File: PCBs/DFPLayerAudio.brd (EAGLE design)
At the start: 45.4 x 33 mm, 14 parts

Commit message: updated something
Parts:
- removed RXTXGND: JST-XH-03-PIN-LONG-PAD, Rembrandt Electronics - JST XH Connectors v1-0:JST-XH-03-PACKAGE-LONG-PAD
- added J2: JST-XH-04-PIN-LONG-PAD, Rembrandt Electronics - JST XH Connectors v1-0:JST-XH-04-PACKAGE-LONG-PAD
- J4: value 6V-12V -> Power
- renumbered 5V to J3, 6V-12V to J4, AMPLIFIER to J1, SPKR1 to LEFTSPKR, SPKR2 to RIGHTSPKR
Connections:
- new net N$6: DFPLAYER.16, J2.2
- new net N$7: J2.3
- net GND: now also J2.1; no longer RXTXGND.1
- net N$2: no longer RXTXGND.2
- net N$8: now also J2.4; no longer RXTXGND.3
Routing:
- net N$8: track 17.7 -> 15.2 mm
- net N$2: track 9.33 -> 8.06 mm
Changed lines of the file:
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@@
 </autorouter>
 <elements>
-<element name="6V-12V" library="SparkFun-Connectors" package="SCREWTERMINAL-5MM-2" value="6V-12V" x="76.2" y="2.54" smashed="yes" rot="R90">
+<element name="J4" library="SparkFun-Connectors" package="SCREWTERMINAL-5MM-2" value="Power" x="76.2" y="2.54" smashed="yes" rot="R90">
 <attribute name="NAME" x="81.28" y="3.81" size="1.27" layer="25" font="vector" ratio="10" rot="R90"/>
 <attribute name="SF_SKU" value="PRT-08432" x="130.81" y="24.13" size="1.778" layer="27" rot="R90" display="off"/>
@@
 <attribute name="VALUE" x="48.26" y="17.78" size="1.27" layer="27" rot="R270" align="top-center"/>
 </element>
-<element name="AMPLIFIER" library="Rembrandt Electronics - JST XH Connectors v1-0" package="JST-XH-03-PACKAGE-LONG-PAD" value="JST-XH-03-PIN-LONG-PAD" x="43.18" y="8.89" smashed="yes" rot="R270">
+<element name="J1" library="Rembrandt Electronics - JST XH Connectors v1-0" package="JST-XH-03-PACKAGE-LONG-PAD" value="JST-XH-03-PIN-LONG-PAD" x="43.18" y="8.89" smashed="yes" rot="R270">
 <attribute name="NAME" x="47.785" y="5.58" size="1.016" layer="25" ratio="10" rot="R90"/>
 <attribute name="VALUE" x="44.5325" y="21.1125" size="1.016" layer="27" ratio="10" rot="R270"/>
 </element>
-<element name="RXTXGND" library="Rembrandt Electronics - JST XH Connectors v1-0" package="JST-XH-03-PACKAGE-LONG-PAD" value="JST-XH-03-PIN-LONG-PAD" x="43.18" y="20.32" smashed="yes" rot="R270">
-<attribute name="NAME" x="47.785" y="17.01" size="1.016" layer="25" ratio="10" rot="R90"/>
-<attribute name="VALUE" x="44.5325" y="22.3825" size="1.016" layer="27" ratio="10" rot="R270"/>
-</element>
-<element name="SPKR1" library="Rembrandt Electronics - JST XH Connectors v1-0" package="JST-XH-02-PACKAGE-LONG-PAD" value="JST-XH-02-PIN-LONG-PAD" x="53.34" y="1.27" smashed="yes">
+<element name="LEFTSPKR" library="Rembrandt Electronics - JST XH Connectors v1-0" package="JST-XH-02-PACKAGE-LONG-PAD" value="JST-XH-02-PIN-LONG-PAD" x="53.34" y="1.27" smashed="yes">
 <attribute name="NAME" x="49.085" y="0.5" size="1.016" layer="25" ratio="10" rot="R90"/>
 <attribute name="VALUE" x="48.7675" y="5.1625" size="1.016" layer="27" ratio="10"/>
 </element>
-<element name="SPKR2" library="Rembrandt Electronics - JST XH Connectors v1-0" package="JST-XH-02-PACKAGE-LONG-PAD" value="JST-XH-02-PIN-LONG-PAD" x="62.23" y="1.27" smashed="yes">
+<element name="RIGHTSPKR" library="Rembrandt Electronics - JST XH Connectors v1-0" package="JST-XH-02-PACKAGE-LONG-PAD" value="JST-XH-02-PIN-LONG-PAD" x="62.23" y="1.27" smashed="yes">
 <attribute name="NAME" x="57.975" y="0.5" size="1.016" layer="25" ratio="10" rot="R90"/>
 <attribute name="VALUE" x="58.9275" y="5.1625" size="1.016" layer="27" ratio="10"/>
@@
 <attribute name="VALUE" x="49.276" y="31.496" size="1.27" layer="27" rot="R180"/>
 </element>
-<element name="5V" library="Rembrandt Electronics - JST XH Connectors v1-0" package="JST-XH-02-PACKAGE-LONG-PAD" value="JST-XH-02-PIN-LONG-PAD" x="81.28" y="12.7" smashed="yes" rot="R90">
+<element name="J3" library="Rembrandt Electronics - JST XH Connectors v1-0" package="JST-XH-02-PACKAGE-LONG-PAD" value="JST-XH-02-PIN-LONG-PAD" x="81.28" y="12.7" smashed="yes" rot="R90">
 <attribute name="NAME" x="83.32" y="8.445" size="1.016" layer="25" ratio="10" rot="R180"/>
 <attribute name="VALUE" x="77.3875" y="9.3975" size="1.016" layer="27" ratio="10" rot="R90"/>
@@
 <attribute name="NAME" x="48.006" y="25.654" size="1.27" layer="25" rot="R180"/>
 <attribute name="VALUE" x="48.006" y="28.956" size="1.27" layer="27" rot="R180"/>
+</element>
+<element name="J2" library="Rembrandt Electronics - JST XH Connectors v1-0" package="JST-XH-04-PACKAGE-LONG-PAD" value="JST-XH-04-PIN-LONG-PAD" x="48.26" y="-7.62" smashed="yes">
+<attribute name="NAME" x="41.605" y="-9.66" size="1.016" layer="25" ratio="10" rot="R90"/>
+<attribute name="VALUE" x="42.2575" y="-3.7275" size="1.016" layer="27" ratio="10"/>
 </element>
 </elements>
@@
 <signal name="GND">
 <contactref element="DFPLAYER" pad="10"/>
-<contactref element="SPKR1" pad="1"/>
-<contactref element="SPKR2" pad="1"/>
+<contactref element="LEFTSPKR" pad="1"/>
+<contactref element="RIGHTSPKR" pad="1"/>
 <contactref element="LED2" pad="C"/>
-<contactref element="6V-12V" pad="2"/>
+<contactref element="J4" pad="2"/>
 <contactref element="7805" pad="3"/>
 <contactref element="C4" pad="2"/>
 <contactref element="C3" pad="2"/>
-<contactref element="AMPLIFIER" pad="2"/>
+<contactref element="J1" pad="2"/>
 <contactref element="DFPLAYER" pad="7"/>
-<contactref element="RXTXGND" pad="1"/>
 <wire x1="73.0758" y1="27.7368" x2="73.0758" y2="26.67" width="0.6096" layer="1"/>
 <wire x1="73.6092" y1="28.2702" x2="73.0758" y2="27.7368" width="0.6096" layer="1"/>
@@
 <wire x1="45.8724" y1="11.2014" x2="45.8724" y2="20.8026" width="0.6096" layer="16"/>
 <wire x1="43.2054" y1="8.5344" x2="45.8724" y2="11.2014" width="0.6096" layer="16"/>
-<wire x1="43.2054" y1="22.4028" x2="43.18" y2="22.86" width="0.6096" layer="16"/>
 <wire x1="43.2054" y1="8.5344" x2="43.18" y2="8.89" width="0.6096" layer="16"/>
 <wire x1="61.341" y1="4.2672" x2="68.2752" y2="11.2014" width="0.6096" layer="16"/>
@@
 <wire x1="61.341" y1="1.6002" x2="60.96" y2="1.27" width="0.6096" layer="16"/>
 <via x="71.4756" y="1.6002" extent="1-16" drill="0.35"/>
-<contactref element="5V" pad="2"/>
+<contactref element="J3" pad="2"/>
 <wire x1="81.0768" y1="19.2024" x2="81.0768" y2="14.4018" width="0.6096" layer="1"/>
 <wire x1="80.01" y1="20.2692" x2="81.0768" y2="19.2024" width="0.6096" layer="1"/>
 <wire x1="81.0768" y1="14.4018" x2="81.28" y2="13.97" width="0.6096" layer="1"/>
 <wire x1="80.01" y1="20.2692" x2="79.97" y2="20.32" width="0.6096" layer="1"/>
+<contactref element="J2" pad="1"/>
+<wire x1="44.45" y1="-7.62" x2="52.07" y2="1.27" width="0" layer="19" extent="1-1"/>
 </signal>
 <signal name="VCC">
@@
 <wire x1="50.8" y1="26.67" x2="51.2064" y2="26.67" width="0.6096" layer="1"/>
 <wire x1="69.8754" y1="4.2672" x2="69.53" y2="3.81" width="0.6096" layer="1"/>
-<contactref element="5V" pad="1"/>
+<contactref element="J3" pad="1"/>
 <wire x1="79.4766" y1="11.2014" x2="81.0768" y2="11.2014" width="0.6096" layer="1"/>
 <wire x1="78.4098" y1="10.1346" x2="79.4766" y2="11.2014" width="0.6096" layer="1"/>
@@
 <signal name="N$14">
 <contactref element="DFPLAYER" pad="5"/>
-<contactref element="AMPLIFIER" pad="1"/>
+<contactref element="J1" pad="1"/>
 <wire x1="47.4726" y1="16.002" x2="50.673" y2="16.002" width="0.6096" layer="1"/>
 <wire x1="43.2054" y1="11.7348" x2="47.4726" y2="16.002" width="0.6096" layer="1"/>
@@
 <signal name="N$12">
 <contactref element="DFPLAYER" pad="8"/>
-<contactref element="SPKR1" pad="2"/>
+<contactref element="LEFTSPKR" pad="2"/>
 <wire x1="51.2064" y1="5.334" x2="51.2064" y2="8.5344" width="0.6096" layer="16"/>
 <wire x1="54.9402" y1="1.6002" x2="51.2064" y2="5.334" width="0.6096" layer="16"/>
@@
 <signal name="N$19">
 <contactref element="DFPLAYER" pad="6"/>
-<contactref element="SPKR2" pad="2"/>
+<contactref element="RIGHTSPKR" pad="2"/>
 <wire x1="61.341" y1="3.7338" x2="51.2064" y2="13.8684" width="0.6096" layer="1"/>
 <wire x1="61.8744" y1="3.7338" x2="61.341" y2="3.7338" width="0.6096" layer="1"/>
@@
 <signal name="N$3">
 <contactref element="7805" pad="1"/>
-<contactref element="6V-12V" pad="1"/>
+<contactref element="J4" pad="1"/>
 <contactref element="C3" pad="1"/>
 <wire x1="74.1426" y1="24.003" x2="74.1426" y2="26.67" width="0.6096" layer="1"/>
@@
 <signal name="N$8">
 <contactref element="R2" pad="2"/>
-<contactref element="RXTXGND" pad="3"/>
 <wire x1="44.196" y1="25.146" x2="44.8056" y2="24.5364" width="0.6096" layer="1"/>
 <wire x1="46.9392" y1="22.4028" x2="44.8056" y2="24.5364" width="0.6096" layer="16"/>
@@
 <wire x1="46.99" y1="21.2852" x2="46.99" y2="19.05" width="0.6096" layer="1"/>
 <wire x1="46.99" y1="19.05" x2="45.72" y2="17.78" width="0.6096" layer="1"/>
-<wire x1="45.72" y1="17.78" x2="43.18" y2="17.78" width="0.6096" layer="1"/>
+<contactref element="J2" pad="4"/>
+<wire x1="52.07" y1="-7.62" x2="45.72" y2="17.78" width="0" layer="19" extent="1-1"/>
 </signal>
 <signal name="N$1">
-<contactref element="AMPLIFIER" pad="3"/>
+<contactref element="J1" pad="3"/>
 <contactref element="DFPLAYER" pad="4"/>
 <wire x1="46.9392" y1="14.9352" x2="50.673" y2="18.669" width="0.6096" layer="16"/>
@@
 </signal>
 <signal name="N$2">
-<contactref element="RXTXGND" pad="2"/>
 <contactref element="R3" pad="2"/>
-<wire x1="43.18" y1="20.32" x2="44.45" y2="20.32" width="0.6096" layer="1"/>
 <wire x1="45.799" y1="21.669" x2="45.799" y2="21.8082875" width="0.6096" layer="1"/>
 <wire x1="46.99" y1="22.9992875" x2="46.99" y2="24.13" width="0.6096" layer="1"/>
@@
 <wire x1="49.53" y1="21.59" x2="50.8" y2="21.59" width="0.6096" layer="1"/>
 </signal>
+<signal name="N$7">
+<contactref element="J2" pad="3"/>
+</signal>
+<signal name="N$6">
+<contactref element="J2" pad="2"/>
+<contactref element="DFPLAYER" pad="16"/>
+<wire x1="46.99" y1="-7.62" x2="68.58" y2="26.67" width="0" layer="19" extent="1-1"/>
+</signal>
 </signals>

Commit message: audio board updated
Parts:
- moved J2 29.2 mm to (44.5, 21.3), turned to 90 degrees
- moved J3 4.31 mm to (78.2, 15.7)
- moved R2 4.19 mm to (52.3, 30.2)
- moved 7805 3.59 mm to (77.0, 23.9)
- moved C3 2.96 mm to (72.1, 29.2)
- moved R3 2.59 mm to (47.5, 29.2)
- moved C4 1.30 mm to (72.4, 14.2), turned to 270 degrees
- moved J4 1.02 mm to (77.2, 2.54)
- moved DFPLAYER 0.51 mm to (59.7, 18.3)
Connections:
- removed net N$2: R3.2
- net N$7: now also R3.2
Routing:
- net N$6: track 0.00 -> 32.4 mm
- net N$7: track 0.00 -> 8.52 mm
- net N$2: track 8.06 -> 0.00 mm
- net GND: track 137.8 -> 132.0 mm
- net VCC: track 66.5 -> 71.9 mm, vias 0 -> 1
- net N$5: track 12.8 -> 9.51 mm
- net N$3: track 28.3 -> 31.5 mm
- net N$4: track 7.01 -> 9.46 mm
- net N$8: track 15.2 -> 12.9 mm, vias 2 -> 0
- net N$1: track 16.8 -> 19.0 mm
- net N$12: track 9.49 -> 10.00 mm
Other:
- board size 45.4 x 33 mm -> 45.4 x 34 mm
- board text added: "Audio Shield V1.0"
- board text added: "Designed & Manufacturd by"
- board text added: "FutureBot"
- board text added: "PINWHEEL ROBOTICS"
- board text added: "Pinwheel Robotics"

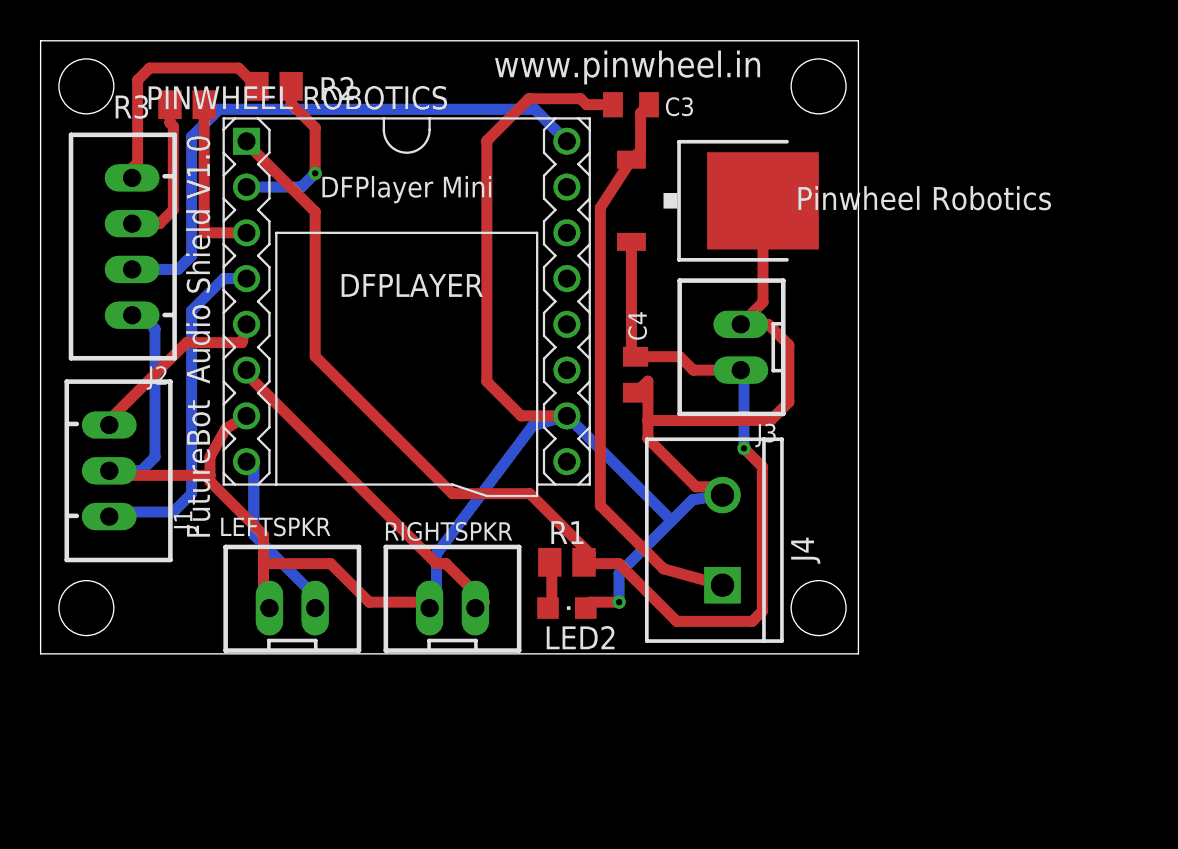
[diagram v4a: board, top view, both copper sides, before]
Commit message: naming part of audio board updated
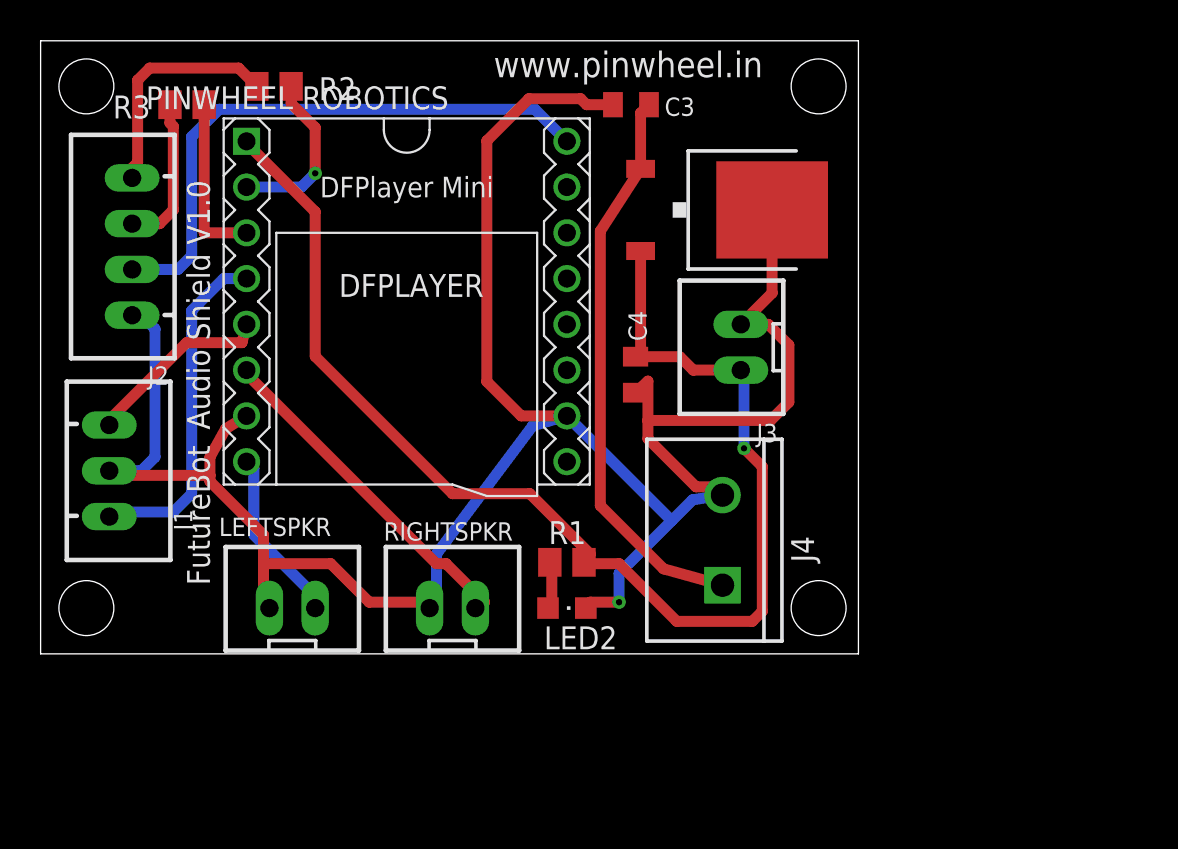
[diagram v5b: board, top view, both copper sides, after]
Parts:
- moved 7805 0.72 mm to (77.5, 23.4)
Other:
- board text added: "17/11/2021"
- board text added: "Documentation at"
- board text added: "FutureBot Audio Shield V1.0"
- board text added: "care@pinwheel.in"

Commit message: updated gerber and corrected few things
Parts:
- renumbered J1 to AMPLIFIER, J2 to UART, J3 to 5V, J4 to 7V-9V
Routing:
- added copper zone on layer 1, net GND
- added copper zone on layer 16, net GND
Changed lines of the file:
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@@
 </autorouter>
 <elements>
-<element name="J4" library="SparkFun-Connectors" package="SCREWTERMINAL-5MM-2" value="Power" x="77.216" y="2.54" smashed="yes" rot="R90">
+<element name="7V-9V" library="SparkFun-Connectors" package="SCREWTERMINAL-5MM-2" value="Power" x="77.216" y="2.54" smashed="yes" rot="R90">
 <attribute name="NAME" x="82.296" y="3.81" size="1.27" layer="25" font="vector" ratio="10" rot="R90"/>
 <attribute name="SF_SKU" value="PRT-08432" x="131.826" y="24.13" size="1.778" layer="27" rot="R90" display="off"/>
@@
 <attribute name="VALUE" x="48.26" y="18.288" size="1.27" layer="27" rot="R270" align="top-center"/>
 </element>
-<element name="J1" library="Rembrandt Electronics - JST XH Connectors v1-0" package="JST-XH-03-PACKAGE-LONG-PAD" value="JST-XH-03-PIN-LONG-PAD" x="43.18" y="8.89" smashed="yes" rot="R270">
-<attribute name="NAME" x="47.785" y="5.58" size="1.016" layer="25" ratio="10" rot="R90"/>
+<element name="AMPLIFIER" library="Rembrandt Electronics - JST XH Connectors v1-0" package="JST-XH-03-PACKAGE-LONG-PAD" value="JST-XH-03-PIN-LONG-PAD" x="43.18" y="8.89" smashed="yes" rot="R270">
+<attribute name="NAME" x="40.673" y="4.056" size="1.016" layer="25" ratio="10" rot="R90"/>
 <attribute name="VALUE" x="46.5645" y="17.5565" size="1.016" layer="27" ratio="10" rot="R270"/>
 </element>
@@
 <attribute name="VALUE" x="53.34" y="32.512" size="1.27" layer="27" rot="R180"/>
 </element>
-<element name="J3" library="Rembrandt Electronics - JST XH Connectors v1-0" package="JST-XH-02-PACKAGE-LONG-PAD" value="JST-XH-02-PIN-LONG-PAD" x="78.232" y="15.748" smashed="yes" rot="R90">
-<attribute name="NAME" x="80.272" y="11.493" size="1.016" layer="25" ratio="10" rot="R180"/>
+<element name="5V" library="Rembrandt Electronics - JST XH Connectors v1-0" package="JST-XH-02-PACKAGE-LONG-PAD" value="JST-XH-02-PIN-LONG-PAD" x="78.232" y="15.748" smashed="yes" rot="R90">
+<attribute name="NAME" x="81.471" y="16.772" size="1.016" layer="25" ratio="10" rot="R270"/>
 <attribute name="VALUE" x="74.3395" y="12.4455" size="1.016" layer="27" ratio="10" rot="R90"/>
 </element>
@@
 <attribute name="VALUE" x="48.514" y="31.496" size="1.27" layer="27" rot="R180"/>
 </element>
-<element name="J2" library="Rembrandt Electronics - JST XH Connectors v1-0" package="JST-XH-04-PACKAGE-LONG-PAD" value="JST-XH-04-PIN-LONG-PAD" x="44.45" y="21.336" smashed="yes" rot="R90">
-<attribute name="NAME" x="46.49" y="14.681" size="1.016" layer="25" ratio="10" rot="R180"/>
+<element name="UART" library="Rembrandt Electronics - JST XH Connectors v1-0" package="JST-XH-04-PACKAGE-LONG-PAD" value="JST-XH-04-PIN-LONG-PAD" x="44.45" y="21.336" smashed="yes" rot="R90">
+<attribute name="NAME" x="39.675" y="19.058" size="1.016" layer="25" ratio="10" rot="R270"/>
 <attribute name="VALUE" x="41.8275" y="17.8735" size="1.016" layer="27" ratio="10" rot="R90"/>
 </element>
@@
 <contactref element="RIGHTSPKR" pad="1"/>
 <contactref element="LED2" pad="C"/>
-<contactref element="J4" pad="2"/>
+<contactref element="7V-9V" pad="2"/>
 <contactref element="7805" pad="3"/>
 <contactref element="C4" pad="2"/>
 <contactref element="C3" pad="2"/>
-<contactref element="J1" pad="2"/>
+<contactref element="AMPLIFIER" pad="2"/>
 <contactref element="DFPLAYER" pad="7"/>
 <wire x1="71.4756" y1="1.6002" x2="69.8754" y2="1.6002" width="0.6096" layer="1"/>
@@
 <wire x1="61.341" y1="1.6002" x2="60.96" y2="1.27" width="0.6096" layer="16"/>
 <via x="71.4756" y="1.6002" extent="1-16" drill="0.35"/>
-<contactref element="J3" pad="2"/>
-<contactref element="J2" pad="1"/>
+<contactref element="5V" pad="2"/>
+<contactref element="UART" pad="1"/>
 <wire x1="44.45" y1="17.526" x2="44.958" y2="17.526" width="0.6096" layer="16"/>
 <wire x1="44.958" y1="17.526" x2="45.72" y2="16.764" width="0.6096" layer="16"/>
@@
 <wire x1="66.04" y1="11.938" x2="64.135" y2="13.843" width="0.6096" layer="1"/>
 <wire x1="64.135" y1="13.843" x2="64.135" y2="27.2034" width="0.6096" layer="1"/>
+<polygon width="0.6096" layer="1" isolate="1.27">
+<vertex x="39.116" y="33.02"/>
+<vertex x="84.836" y="33.02"/>
+<vertex x="84.836" y="-1.524"/>
+<vertex x="39.116" y="-1.524"/>
+</polygon>
+<polygon width="0.6096" layer="16" isolate="1.27">
+<vertex x="39.624" y="32.512"/>
+<vertex x="84.328" y="32.512"/>
+<vertex x="84.836" y="32.004"/>
+<vertex x="84.836" y="-1.016"/>
+<vertex x="39.116" y="-1.016"/>
+<vertex x="39.116" y="32.512"/>
+</polygon>
 </signal>
 <signal name="VCC">
@@
 <wire x1="50.8" y1="27.178" x2="50.8" y2="27.0764" width="0.6096" layer="1"/>
 <wire x1="69.8754" y1="4.2672" x2="69.53" y2="3.81" width="0.6096" layer="1"/>
-<contactref element="J3" pad="1"/>
+<contactref element="5V" pad="1"/>
 <wire x1="75.5904" y1="14.478" x2="78.232" y2="14.478" width="0.6096" layer="1"/>
 <wire x1="54.61" y1="23.2664" x2="54.61" y2="15.24" width="0.6096" layer="1"/>
@@
 <signal name="N$14">
 <contactref element="DFPLAYER" pad="5"/>
-<contactref element="J1" pad="1"/>
+<contactref element="AMPLIFIER" pad="1"/>
 <wire x1="47.4726" y1="16.002" x2="50.546" y2="16.002" width="0.6096" layer="1"/>
 <wire x1="43.2054" y1="11.7348" x2="47.4726" y2="16.002" width="0.6096" layer="1"/>
@@
 <signal name="N$3">
 <contactref element="7805" pad="1"/>
-<contactref element="J4" pad="1"/>
+<contactref element="7V-9V" pad="1"/>
 <contactref element="C3" pad="1"/>
 <wire x1="73.136" y1="29.21" x2="72.67" y2="28.744" width="0.6096" layer="1"/>
@@
 <wire x1="50.358" y1="31.242" x2="51.374" y2="30.226" width="0.6096" layer="1"/>
 <wire x1="50.358" y1="31.242" x2="45.42515625" y2="31.242" width="0.6096" layer="1"/>
-<contactref element="J2" pad="4"/>
+<contactref element="UART" pad="4"/>
 <wire x1="44.45" y1="25.69484375" x2="44.7548" y2="25.99964375" width="0.6096" layer="1"/>
 <wire x1="44.7548" y1="30.57164375" x2="45.42515625" y2="31.242" width="0.6096" layer="1"/>
@@
 </signal>
 <signal name="N$1">
-<contactref element="J1" pad="3"/>
+<contactref element="AMPLIFIER" pad="3"/>
 <contactref element="DFPLAYER" pad="4"/>
 <wire x1="43.18" y1="6.35" x2="43.434" y2="6.604" width="0.6096" layer="16"/>
@@
 </signal>
 <signal name="N$7">
-<contactref element="J2" pad="3"/>
+<contactref element="UART" pad="3"/>
 <contactref element="R3" pad="2"/>
 <wire x1="46.736" y1="28.006" x2="46.548" y2="28.194" width="0.6096" layer="1"/>
@@
 </signal>
 <signal name="N$6">
-<contactref element="J2" pad="2"/>
+<contactref element="UART" pad="2"/>
 <contactref element="DFPLAYER" pad="16"/>
 <wire x1="68.58" y1="27.178" x2="66.802" y2="28.956" width="0.6096" layer="16"/>
